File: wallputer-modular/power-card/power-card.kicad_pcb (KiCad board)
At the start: 2 copper layers, 139 parts, among them J2 Power, Q1 FQP27P06, Q2 IRLZ44N, SW1 reset, U1 TLC555CD, U12 74HC04, U16 74HC04, U17 74HC04, U18 74HC04, U2 74HC04, U3 74HC04

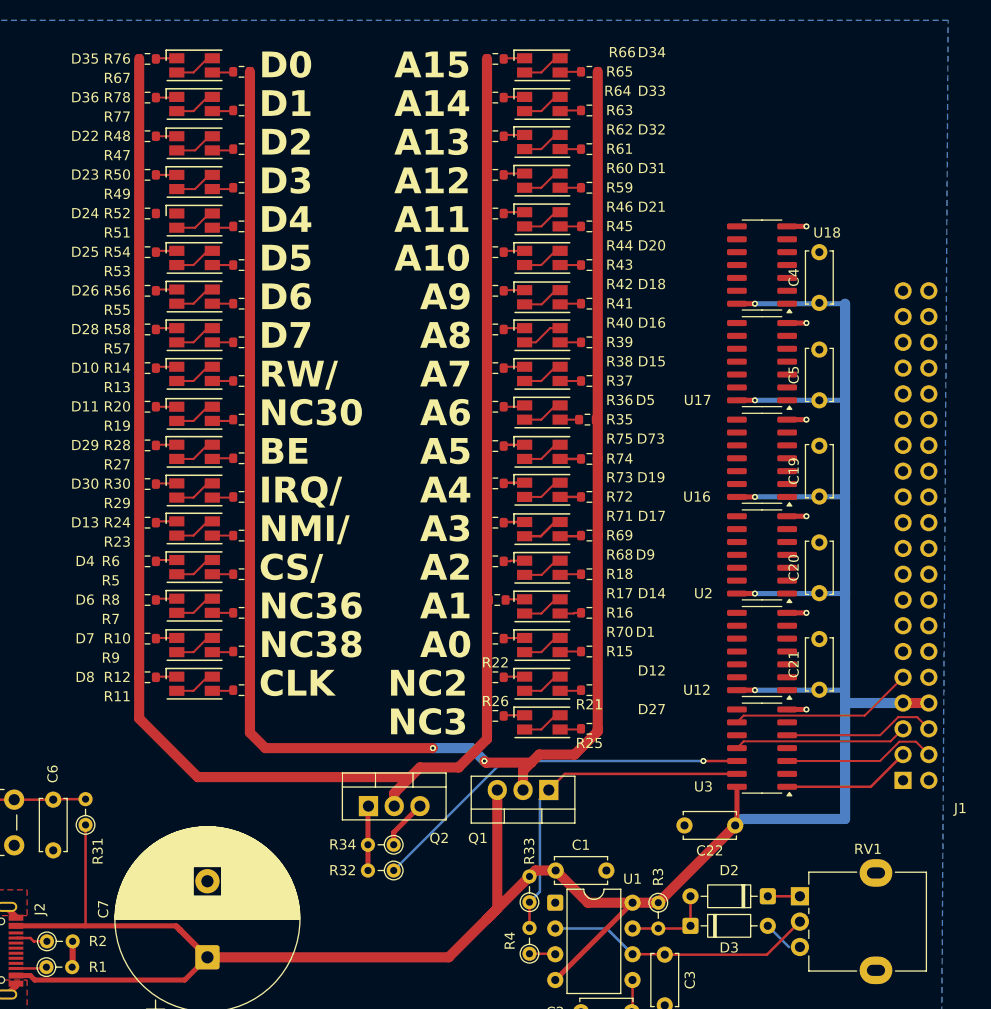
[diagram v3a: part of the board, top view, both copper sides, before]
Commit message: finish wiring pcb
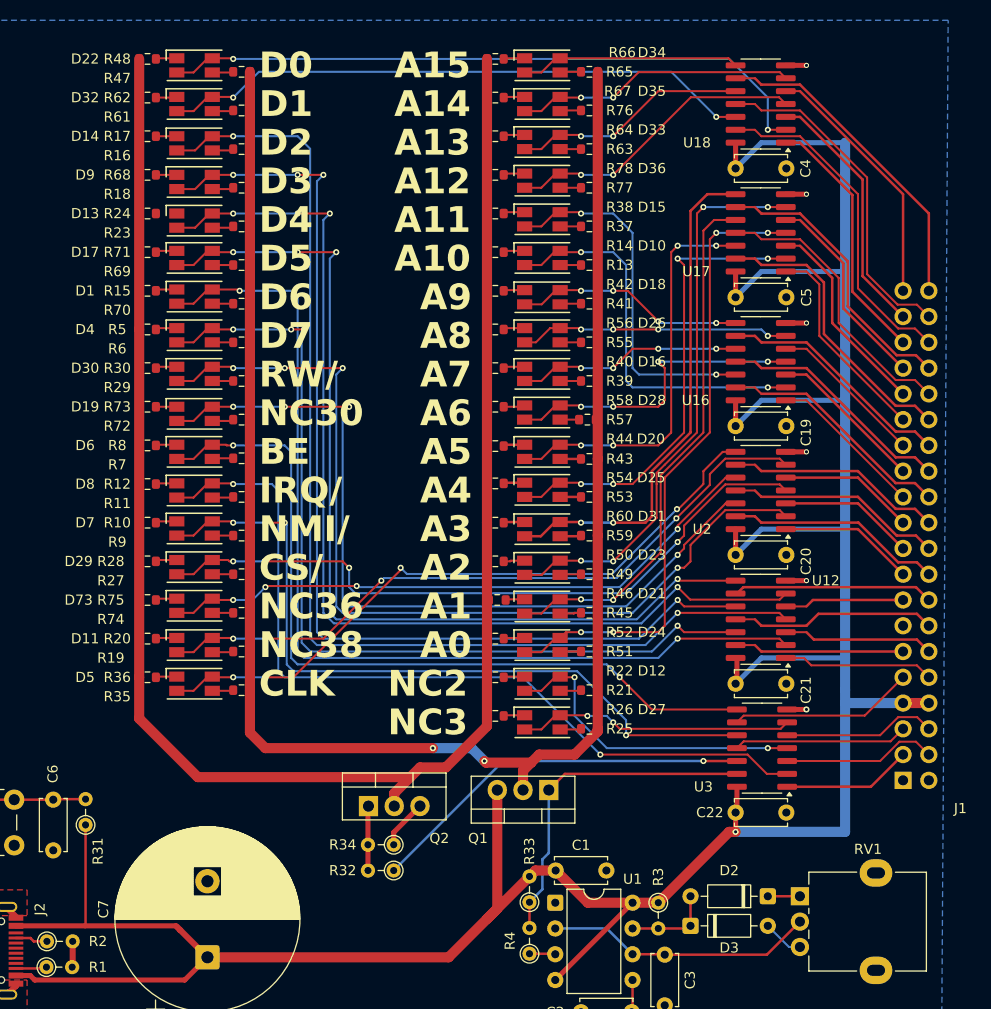
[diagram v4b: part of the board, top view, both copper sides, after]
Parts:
- moved U18 15.9 mm to (147.3, 71.8)
- moved C4 15.6 mm to (144.8, 78.1), turned to 0 degrees
- moved C5 13.1 mm to (144.8, 90.8), turned to 0 degrees
- moved U17 12.7 mm to (147.3, 84.5)
- moved C19 10.8 mm to (144.8, 103.5), turned to 0 degrees
- moved U16 9.53 mm to (147.3, 97.2)
- moved C20 9.08 mm to (144.8, 116.2), turned to 0 degrees
- moved C21 8.28 mm to (144.8, 128.9), turned to 0 degrees
- moved U2 6.35 mm to (147.3, 109.9)
- moved U12 3.18 mm to (147.3, 122.6)
- moved C22 1.27 mm to (144.8, 141.6), turned to 0 degrees
- renumbered D26 to D1, D20 to D10, D7 to D11, D24 to D13, D22 to D14, D21 to D15, D15 to D16, D25 to D17, D11 to D19, D73 to D20, D14 to D21, D35 to D22, D9 to D23, D1 to D24, D19 to D25, D16 to D26, D5 to D28, D4 to D29, D10 to D30, D17 to D31, D36 to D32, D32 to D33, D33 to D35, D31 to D36, D28 to D4, D8 to D5, D29 to D6, D13 to D7, D6 to D73, D30 to D8, D23 to D9, R24 to R10, R29 to R11, R30 to R12, R43 to R13, R44 to R14, R56 to R15, R47 to R16, R48 to R17, R49 to R18, R9 to R19, R10 to R20, R51 to R23, R52 to R24, R5 to R27, R6 to R28, R13 to R29, R14 to R30, R11 to R35, R12 to R36, R45 to R37, R46 to R38, R37 to R39, R38 to R40, R74 to R43, R75 to R44, R16 to R45, R17 to R46, R67 to R47, R76 to R48, R18 to R49, R58 to R5, R68 to R50, R15 to R51, R70 to R52, R72 to R53, R73 to R54, R39 to R55, R40 to R56, R35 to R57, R36 to R58, R69 to R59, R57 to R6, R71 to R60, R77 to R61, R78 to R62, R61 to R63, R62 to R64, R64 to R67, R50 to R68, R53 to R69, R27 to R7, R55 to R70, R54 to R71, R19 to R72, R20 to R73, R7 to R74, R8 to R75, R63 to R76, R59 to R77, R60 to R78, R28 to R8, R23 to R9
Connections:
- net /A3 renamed A3
- net /A9 renamed A9
- D10 pad 1: Net-(D20-Green_A) -> Net-(D10-Green_A)
- D10 pad 3: Net-(D20-Green_A) -> Net-(D10-Green_A)
- D13 pad 1: Net-(D24-Green_A) -> Net-(D13-Green_A)
- D13 pad 3: Net-(D24-Green_A) -> Net-(D13-Green_A)
- D14 pad 1: Net-(D22-Green_A) (its old number) -> Net-(D14-Green_A)
- D14 pad 3: Net-(D22-Green_A) (its old number) -> Net-(D14-Green_A)
- D15 pad 1: Net-(D21-Green_A) -> Net-(D15-Green_A)
- D15 pad 3: Net-(D21-Green_A) -> Net-(D15-Green_A)
- D17 pad 1: Net-(D25-Green_A) -> Net-(D17-Green_A)
- D17 pad 3: Net-(D25-Green_A) -> Net-(D17-Green_A)
- D20 pad 1: Net-(D73-Green_A) (its old number) -> Net-(D20-Green_A)
- D20 pad 3: Net-(D73-Green_A) (its old number) -> Net-(D20-Green_A)
- D21 pad 1: Net-(D14-Green_A) -> Net-(D21-Green_A)
- D21 pad 3: Net-(D14-Green_A) -> Net-(D21-Green_A)
- D23 pad 1: Net-(D9-Green_A) -> Net-(D23-Green_A)
- D23 pad 3: Net-(D9-Green_A) -> Net-(D23-Green_A)
- D24 pad 1: Net-(D1-Green_A) (its old number) -> Net-(D24-Green_A)
- D24 pad 3: Net-(D1-Green_A) (its old number) -> Net-(D24-Green_A)
- D25 pad 1: Net-(D19-Green_A) (its old number) -> Net-(D25-Green_A)
- D25 pad 3: Net-(D19-Green_A) (its old number) -> Net-(D25-Green_A)
- D31 pad 1: Net-(D17-Green_A) -> Net-(D31-Green_A)
- D31 pad 3: Net-(D17-Green_A) -> Net-(D31-Green_A)
- D33 pad 1: Net-(D32-Green_A) (its old number) -> Net-(D33-Green_A)
- D33 pad 3: Net-(D32-Green_A) (its old number) -> Net-(D33-Green_A)
- D35 pad 1: Net-(D33-Green_A) -> Net-(D35-Green_A)
- D35 pad 3: Net-(D33-Green_A) -> Net-(D35-Green_A)
- D36 pad 1: Net-(D31-Green_A) -> Net-(D36-Green_A)
- D36 pad 3: Net-(D31-Green_A) -> Net-(D36-Green_A)
- D9 pad 1: Net-(D23-Green_A) -> Net-(D9-Green_A)
- D9 pad 3: Net-(D23-Green_A) -> Net-(D9-Green_A)
- J1 pad 10: /A5 -> A5
- J1 pad 11: /A6 -> A6
- J1 pad 12: /A7 -> A7
- J1 pad 13: /A8 -> A8
- J1 pad 15: /A10 -> A10
- J1 pad 16: /A11 -> A11
- J1 pad 17: /A12 -> A12
- J1 pad 18: /A13 -> A13
- J1 pad 19: /A14 -> A14
- J1 pad 20: /A15 -> A15
- J1 pad 21: /D0 -> D0
- J1 pad 22: /D1 -> D1
- J1 pad 23: /D2 -> D2
- J1 pad 24: /D3 -> D3
- J1 pad 25: /D4 -> D4
- J1 pad 26: /D5 -> D5
- J1 pad 27: /D6 -> D6
- J1 pad 28: /D7 -> D7
- J1 pad 32: IRQ -> IRQ/
- J1 pad 33: NMI -> NMI/
- J1 pad 34: RES -> RES/
- J1 pad 5: /A0 -> A0
- J1 pad 6: /A1 -> A1
- J1 pad 7: /A2 -> A2
- J1 pad 9: /A4 -> A4
- U12 pad 1: /D6 -> A0
- U12 pad 10: Net-(D14-Green_A) -> Net-(D9-Green_A)
- U12 pad 11: /A1 -> A2
- U12 pad 13: /D7 -> CS/
- U12 pad 3: /A0 -> A1
- U12 pad 4: Net-(D1-Green_A) (its old number) -> Net-(D14-Green_A)
- U12 pad 5: /A2 -> NMI/
- U12 pad 6: Net-(D9-Green_A) -> Net-(D13-Green_A)
- U16 pad 1: /A4 -> RW/
- U16 pad 11: /A7 -> A8
- U16 pad 12: Net-(D73-Green_A) (its old number) -> Net-(D15-Green_A)
- U16 pad 13: /A5 -> A7
- U16 pad 2: Net-(D19-Green_A) (its old number) -> Net-(D10-Green_A)
- U16 pad 3: /A6 -> D7
- U16 pad 5: /A8 -> D6
- U17 pad 1: /A10 -> D5
- U17 pad 10: Net-(D32-Green_A) (its old number) -> Net-(D21-Green_A)
- U17 pad 11: /A13 -> A11
- U17 pad 12: Net-(D21-Green_A) -> Net-(D20-Green_A)
- U17 pad 13: /A11 -> A10
- U17 pad 2: Net-(D20-Green_A) -> Net-(D25-Green_A)
- U17 pad 3: /A12 -> D4
- U17 pad 4: Net-(D31-Green_A) -> Net-(D24-Green_A)
- U17 pad 5: /A14 -> D3
- U17 pad 6: Net-(D33-Green_A) -> Net-(D23-Green_A)
- U17 pad 8: Net-(D34-Green_A) -> Net-(D31-Green_A)
- U17 pad 9: /A15 -> A12
- U18 pad 1: /D0 -> D2
- U18 pad 10: Net-(D23-Green_A) -> Net-(D33-Green_A)
- U18 pad 11: /D3 -> A14
- U18 pad 13: /D1 -> A13
- U18 pad 3: /D2 -> D1
- U18 pad 4: Net-(D22-Green_A) (its old number) -> Net-(D36-Green_A)
- U18 pad 5: /D4 -> D0
- U18 pad 6: Net-(D24-Green_A) -> Net-(D35-Green_A)
- U18 pad 8: Net-(D25-Green_A) -> Net-(D34-Green_A)
- U18 pad 9: /D5 -> A15
- U2 pad 1: RW/ -> IRQ/
- U2 pad 11: CS/ -> A5
- U2 pad 13: NC3 -> A4
- U2 pad 5: IRQ -> NC30
- U2 pad 9: NMI -> A6
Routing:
- net Net-(D14-Green_A): track 4.08 -> 111.2 mm, vias 0 -> 2
- net Net-(D13-Green_A): track 0.00 -> 103.6 mm, vias 0 -> 4
- net Net-(D9-Green_A): track 4.08 -> 103.8 mm, vias 0 -> 4
- net Net-(D1-Green_A): track 4.08 -> 97.2 mm, vias 0 -> 2
- net Net-(D17-Green_A): track 4.08 -> 94.6 mm, vias 0 -> 4
- net Net-(D30-Green_A): track 4.08 -> 90.7 mm, vias 0 -> 4
- net Net-(D4-Green_A): track 4.53 -> 89.1 mm, vias 0 -> 4
- net Net-(D8-Green_A): track 4.08 -> 83.0 mm, vias 0 -> 2
- net Net-(D19-Green_A): track 4.08 -> 80.3 mm, vias 0 -> 4
- net Net-(D6-Green_A): track 4.08 -> 78.5 mm, vias 0 -> 2
- net Net-(D7-Green_A): track 4.08 -> 73.5 mm, vias 0 -> 4
- net Net-(D11-Green_A): track 4.08 -> 68.9 mm, vias 0 -> 4
- net Net-(D29-Green_A): track 4.08 -> 68.4 mm, vias 0 -> 4
- net Net-(D5-Green_A): track 4.08 -> 66.3 mm, vias 0 -> 4
- net Net-(D22-Green_A): track 4.08 -> 65.4 mm, vias 0 -> 2
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
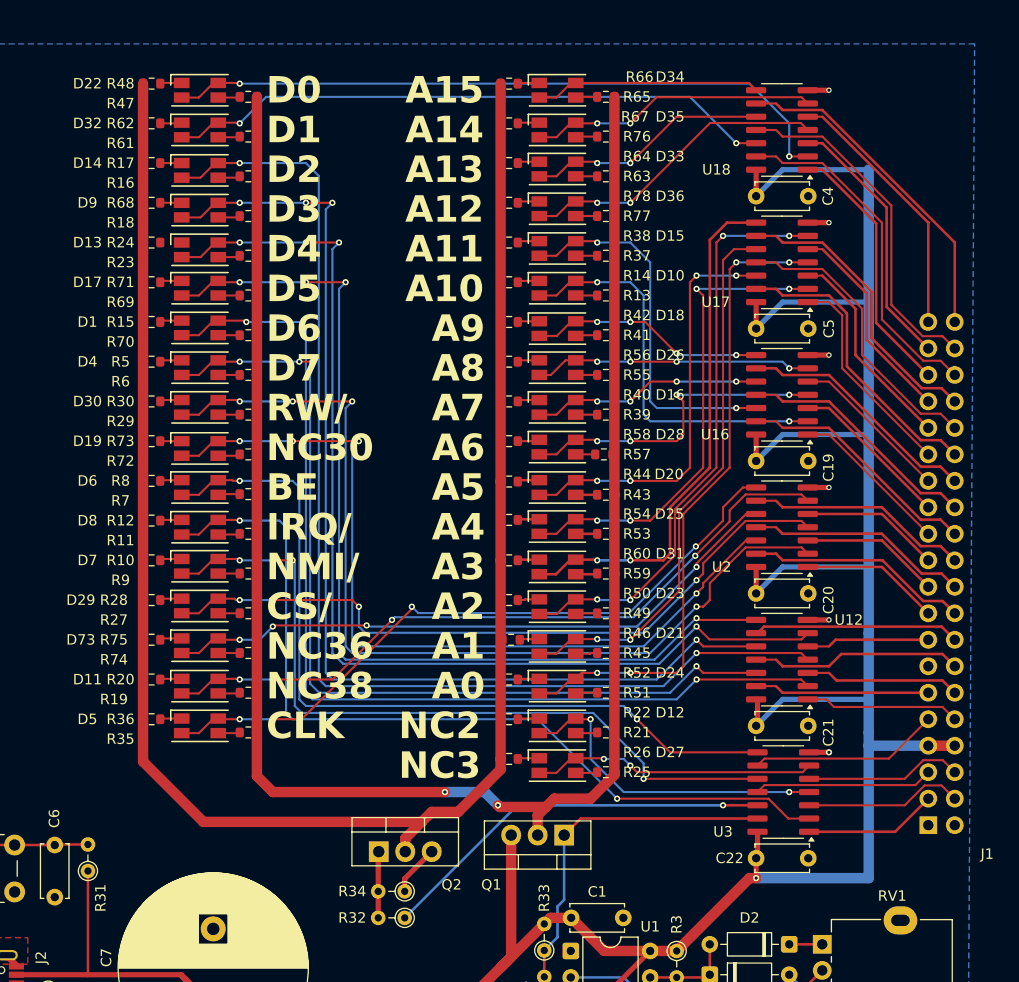
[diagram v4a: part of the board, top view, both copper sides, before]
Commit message: redesigning traces
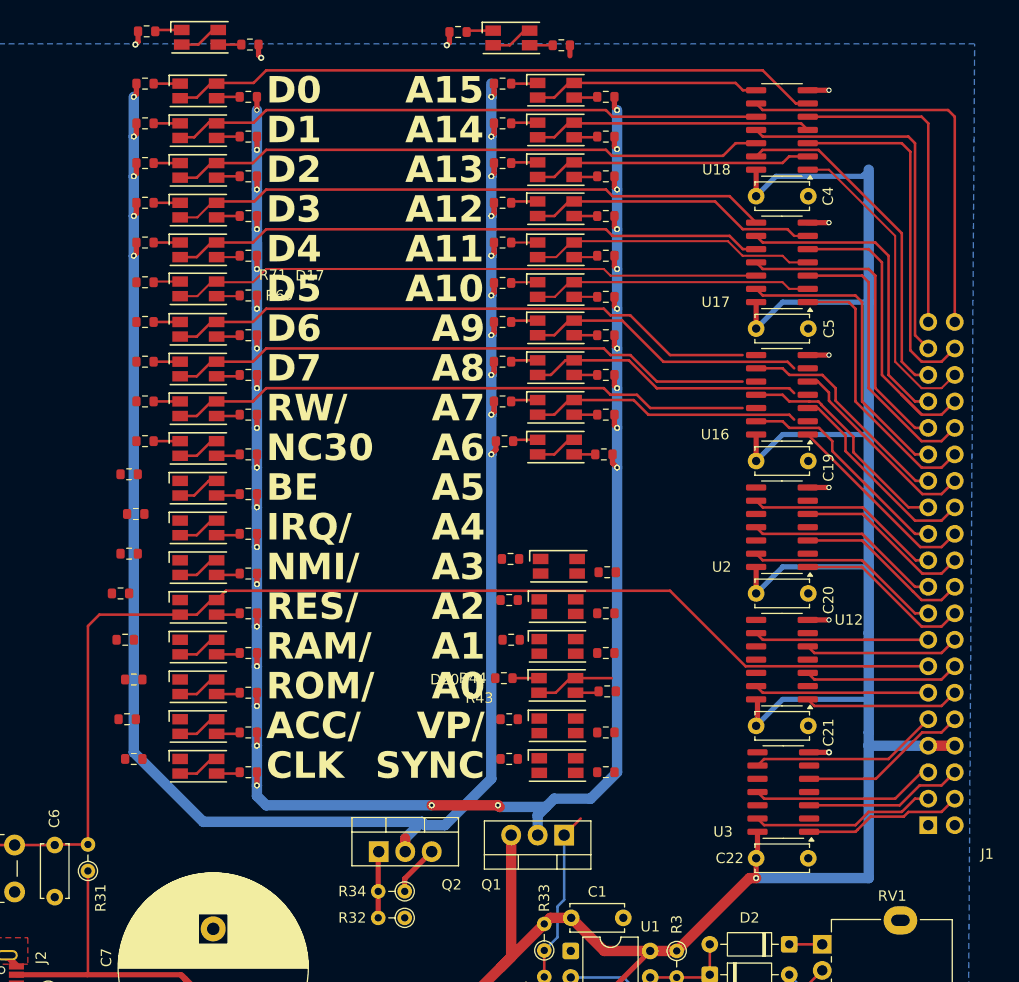
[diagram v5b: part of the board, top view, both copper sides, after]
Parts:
- removed R23: 680, Resistor_SMD:R_0603_1608Metric
- added D37: Wallputer_Dual_LED, Wallputer:Wallputer_Dual_LED, F.Cu at (91.3, 117.5)
- added R79: 680, Resistor_SMD:R_0603_1608Metric, F.Cu at (96.1, 118.1)
- added R80: 680, Resistor_SMD:R_0603_1608Metric, F.Cu at (83.8, 116.2)
- added R81: 680, Resistor_SMD:R_0603_1608Metric, F.Cu at (96.1, 83.8)
- moved R43 51.2 mm to (130.5, 125.6)
- moved D20 51.2 mm to (125.7, 125.0)
- moved R44 50.8 mm to (120.6, 124.3)
- moved R60 48.9 mm to (86.2, 78.7)
- moved D31 48.6 mm to (91.3, 79.4)
- moved D9 48.5 mm to (125.9, 113.6)
- moved R18 48.5 mm to (130.5, 114.2)
- moved R68 48.5 mm to (121.2, 112.9)
- moved R59 48.5 mm to (96.1, 80.0)
- moved R52 41.9 mm to (120.5, 82.5)
- moved R51 41.9 mm to (130.4, 83.8)
- moved D15 41.8 mm to (125.6, 83.2)
- moved R38 40.2 mm to (86.3, 62.3)
- moved D24 39.8 mm to (91.4, 62.9)
- moved R71 39.8 mm to (86.2, 86.4)
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- renumbered D24 to D15, D20 to D17, D17 to D20, D15 to D24, R69 to R43, R71 to R44, R43 to R69, R44 to R71
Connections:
- net CS/ renamed RAM/
- net NC36 renamed ROM/
- net NC38 renamed ACC/
- C6 pad 1: RES -> RES/
- J1 pad 2: NC2 -> SYNC
- J1 pad 3: NC3 -> VP/
- R31 pad 2: RES -> RES/
- SW1 pad 1: RES -> RES/
- U12 pad 1: A0 -> A1
- U12 pad 10: Net-(D9-Green_A) -> Net-(R32-Pad1)
- U12 pad 11: A2 -> SW_BUS_LED
- U12 pad 3: A1 -> A2
- U12 pad 4: Net-(D14-Green_A) -> Net-(D23-Green_A)
- U12 pad 5: NMI/ -> A3
- U12 pad 6: Net-(D13-Green_A) -> Net-(D21-Green_A)
- U12 pad 9: A3 -> NMI/
- U16 pad 1: RW/ -> A7
- U16 pad 11: A8 -> D7
- U16 pad 13: A7 -> RW/
- U16 pad 3: D7 -> A8
- U16 pad 5: D6 -> A9
- U16 pad 9: A9 -> D6
- U17 pad 1: D5 -> A10
- U17 pad 10: Net-(D21-Green_A) -> Net-(D13-Green_A)
- U17 pad 11: A11 -> D4
- U17 pad 13: A10 -> D5
- U17 pad 3: D4 -> A11
- U17 pad 5: D3 -> A12
- U17 pad 6: Net-(D23-Green_A) -> Net-(D36-Green_A)
- U17 pad 9: A12 -> D3
- U18 pad 1: D2 -> A13
- U18 pad 10: Net-(D33-Green_A) -> Net-(D32-Green_A)
- U18 pad 11: A14 -> D1
- U18 pad 12: Net-(D32-Green_A) -> Net-(D14-Green_A)
- U18 pad 13: A13 -> D2
- U18 pad 2: Net-(D22-Green_A) -> Net-(D33-Green_A)
- U18 pad 3: D1 -> A14
- U18 pad 4: Net-(D36-Green_A) -> Net-(D35-Green_A)
- U18 pad 6: Net-(D35-Green_A) -> Net-(D22-Green_A)
- U2 pad 1: IRQ/ -> A4
- U2 pad 11: A5 -> BE
- U2 pad 13: A4 -> IRQ/
- U2 pad 3: BE -> A5
- U2 pad 5: NC30 -> A6
- U2 pad 9: A6 -> NC30
- U3 pad 1: CLK -> SYNC
- U3 pad 12: Net-(R32-Pad1) -> Net-(D9-Green_A)
- U3 pad 13: SW_BUS_LED -> CLK
- U3 pad 3: NC2 -> VP/
- U3 pad 5: NC3 -> A0
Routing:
- net RES/: track 0.00 -> 119.8 mm
- net Net-(D9-Green_A): track 103.8 -> 0.00 mm, vias 4 -> 0
- net Net-(D20-Green_A): track 94.6 -> 7.56 mm, vias 4 -> 0
- net Net-(D8-Green_A): track 83.0 -> 4.08 mm, vias 2 -> 0
- net Net-(D19-Green_A): track 80.3 -> 4.08 mm, vias 4 -> 0
- net Net-(D6-Green_A): track 78.5 -> 4.08 mm, vias 2 -> 0
- net Net-(D7-Green_A): track 73.5 -> 4.08 mm, vias 4 -> 0
- net Net-(D11-Green_A): track 68.9 -> 4.08 mm, vias 4 -> 0
- net Net-(D29-Green_A): track 68.4 -> 4.08 mm, vias 4 -> 0
- net Net-(D5-Green_A): track 66.3 -> 4.08 mm, vias 4 -> 0
- net Net-(D73-Green_A): track 61.0 -> 4.08 mm, vias 4 -> 0
- net Net-(D23-Green_A): track 56.1 -> 0.00 mm, vias 4 -> 0
- net Net-(D14-Green_A): track 111.2 -> 57.4 mm, vias 2 -> 0
- net Net-(D21-Green_A): track 53.0 -> 0.00 mm, vias 2 -> 0
- net Net-(D13-Green_A): track 103.6 -> 57.1 mm, vias 4 -> 0
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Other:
- board text added: "ACC/"
- board text added: "RAM/"
- board text added: "RES/"
- board text added: "ROM/"
- board text added: "SYNC"
- board text added: "VP/"
- board text removed: "CS/"
- board text removed: "NC2"
- board text removed: "NC3"
- board text removed: "NC36"
- board text removed: "NC38"

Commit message: more routing
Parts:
- moved R18 62.8 mm to (79.6, 77.4)
- moved D9 62.8 mm to (74.9, 76.8)
- moved R68 62.8 mm to (70.3, 76.1)
- moved D1 45.9 mm to (125.6, 121.3)
- moved R15 45.9 mm to (120.5, 120.7)
- moved R70 45.7 mm to (130.2, 121.9)
- moved R28 44.3 mm to (120.5, 105.4)
- moved D29 43.5 mm to (125.6, 106.0)
- moved R27 43.3 mm to (130.2, 106.6)
- moved R20 42.1 mm to (120.5, 101.6)
- moved D11 41.2 mm to (125.6, 102.2)
- moved R19 41.1 mm to (130.2, 102.8)
- moved D20 36.2 mm to (91.3, 113.7)
- moved R43 36.2 mm to (96.1, 114.2)
- moved R44 36.2 mm to (86.2, 113.0)
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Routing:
- net Net-(D20-Green_A): track 7.56 -> 66.8 mm
- net Net-(D5-Green_A): track 4.08 -> 62.8 mm
- net Net-(D24-Green_A): track 4.08 -> 61.2 mm
- net Net-(D73-Green_A): track 4.08 -> 58.2 mm
- net Net-(D19-Green_A): track 4.08 -> 57.6 mm
- net Net-(D16-Green_A): track 25.8 -> 57.7 mm
- net Net-(D18-Green_A): track 27.1 -> 58.2 mm
- net Net-(D23-Green_A): track 0.00 -> 29.4 mm
- net Net-(D21-Green_A): track 0.00 -> 29.1 mm
- net Net-(D11-Green_A): track 4.08 -> 33.0 mm
- net Net-(D1-Green_A): track 56.9 -> 28.3 mm
- net Net-(D29-Green_A): track 4.08 -> 32.4 mm
- net Net-(D30-Green_A): track 55.8 -> 27.8 mm
- net Net-(D10-Green_A): track 4.08 -> 31.3 mm
- net Net-(D28-Green_A): track 4.08 -> 27.7 mm
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
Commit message: finish routing
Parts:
- moved R18 58.3 mm to (96.1, 133.3)
- moved D9 58.3 mm to (91.3, 132.8)
- moved R68 58.2 mm to (86.2, 132.1)
- moved D8 53.7 mm to (125.6, 132.8)
- moved R12 53.7 mm to (120.5, 132.1)
- moved R11 53.5 mm to (130.2, 133.3)
- moved R7 21.0 mm to (96.1, 125.7)
- moved D6 21.0 mm to (91.3, 125.1)
- moved R8 21.0 mm to (86.2, 124.4)
- moved R10 19.3 mm to (86.2, 128.3)
- moved R9 19.3 mm to (96.1, 129.5)
- moved D7 19.3 mm to (91.3, 128.9)
- moved R26 7.65 mm to (120.5, 124.5)
- moved R25 7.62 mm to (130.2, 125.7)
- moved D27 7.62 mm to (125.6, 125.1)
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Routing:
- net Net-(D6-Green_A): track 0.00 -> 59.9 mm
- net Net-(D7-Green_A): track 0.00 -> 59.3 mm
- net Net-(D9-Green_A): track 0.00 -> 58.8 mm
- net Net-(R32-Pad1): track 0.00 -> 52.4 mm, vias 0 -> 2
- net SW_BUS_LED: track 16.6 -> 47.7 mm, vias 0 -> 2
- net Net-(D27-Green_A): track 0.00 -> 30.1 mm
- net Net-(D12-Green_A): track 0.00 -> 29.5 mm
- net Net-(D8-Green_A): track 0.00 -> 29.0 mm
- net Net-(Q2-D): track 206.5 -> 221.3 mm, vias 25 -> 36
- net Net-(Q1-D): track 209.9 -> 219.2 mm, vias 31 -> 38
- net Net-(D20-Green_A): track 66.8 -> 59.3 mm
- net Net-(D10-Green_A): track 31.3 -> 27.2 mm
- net Net-(D11-Green_A): track 33.0 -> 28.9 mm
- net Net-(D24-Green_A): track 61.2 -> 57.1 mm
- net Net-(D29-Green_A): track 32.4 -> 28.4 mm
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
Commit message: clean up routing
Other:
- board text added: "LED Brightness"
- board text added: "RESET"
